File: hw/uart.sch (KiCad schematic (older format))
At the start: 10 parts

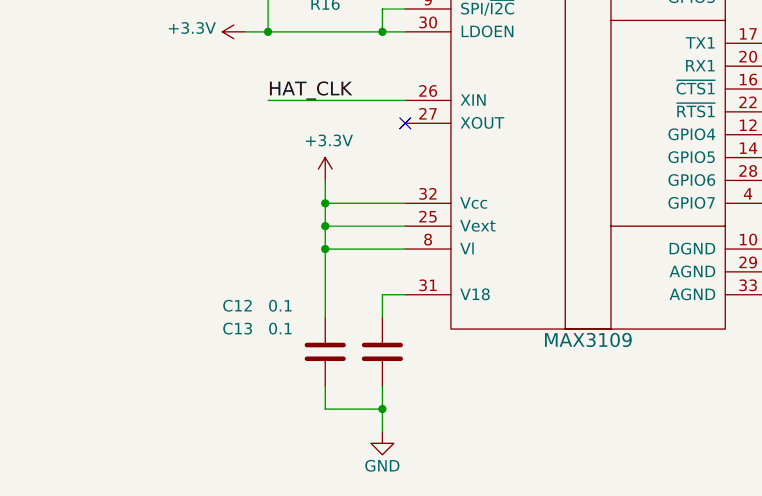
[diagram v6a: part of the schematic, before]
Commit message: hw: remove header with unused rpi gpio's, more net labels
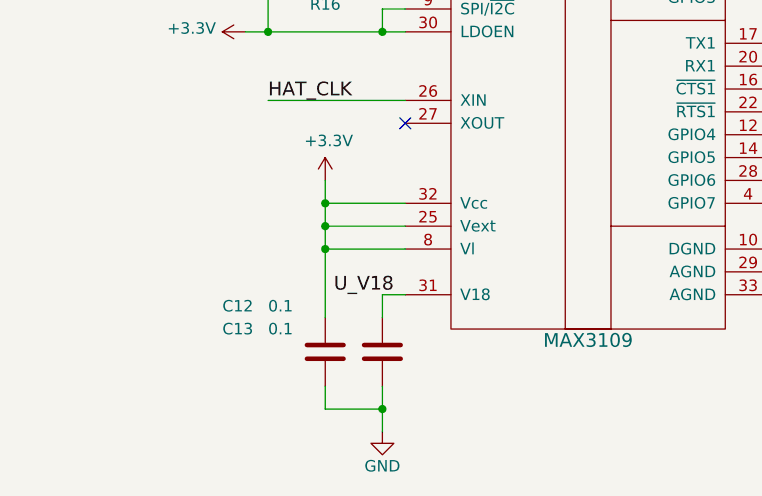
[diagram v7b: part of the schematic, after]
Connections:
- net U_V18: now reaches C13.1, DD4.31 (V18)
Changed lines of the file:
@@
 $EndComp
 $Comp
-L power:GND #PWR?
+L power:GND #PWR0104
 U 1 1 5ACF9FBD
 P 6650 7350
-F 0 "#PWR?" H 6650 7100 50  0001 C CNN
+F 0 "#PWR0104" H 6650 7100 50  0001 C CNN
 F 1 "GND" H 6650 7200 50  0000 C CNN
 F 2 "" H 6650 7350 50  0001 C CNN
@@
 $EndComp
 $Comp
-L power:GND #PWR?
+L power:GND #PWR0105
 U 1 1 5ACFA00F
 P 6900 6450
-F 0 "#PWR?" H 6900 6200 50  0001 C CNN
+F 0 "#PWR0105" H 6900 6200 50  0001 C CNN
 F 1 "GND" H 6900 6300 50  0000 C CNN
 F 2 "" H 6900 6450 50  0001 C CNN
@@
 Wire Wire Line
 	6650 7350 6650 7250
+Text Label 3400 7600 2    60   ~ 0
+U_V18
 $EndSCHEMATC
